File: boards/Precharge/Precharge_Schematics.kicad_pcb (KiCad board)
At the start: 2 copper layers, 67 x 43 mm, 5 parts, among them J1 Ultrafit_2, J2 Ultrafit_2, J3 Ultrafit_2, K1 G2RL-1-E

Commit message: Updated Layout
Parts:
- moved J2 5.53 mm to (178.5, 89.9), turned to 270 degrees
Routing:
- net Low_Side_Drive: track 21.5 -> 7.29 mm
- net Shutdown_in: track 5.04 -> 16.1 mm
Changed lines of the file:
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@@
     (links 5)
     (no_connects 2)
-    (area 123.418599 67.540599 179.359401 114.8118)
+    (area 115.672399 67.247203 182.772401 110.384035)
     (thickness 1.6)
     (drawings 36)
-    (tracks 13)
+    (tracks 14)
     (zones 0)
     (modules 5)
@@
   )
   (setup
-    (last_trace_width 0.254)
+    (last_trace_width 0.762)
     (user_trace_width 0.254)
     (user_trace_width 0.508)
@@
   )
   (module footprints:Ultrafit_2 (layer F.Cu)
-    (at 173.482 87.63 90)
-    (fp_text reference J2 (at 9.0678 0.5917 90) (layer F.SilkS) hide
-      (effects (font (size 1 1) (thickness 0.15)))
-    )
-    (fp_text value Ultrafit_2 (at 4.572 0.508 180) (layer F.Fab) hide
+    (at 178.5366 89.8652 270)
+    (fp_text reference J2 (at 9.0678 0.5917 270) (layer F.SilkS) hide
+      (effects (font (size 1 1) (thickness 0.15)))
+    )
+    (fp_text value Ultrafit_2 (at 4.572 0.508 360) (layer F.Fab) hide
       (effects (font (size 1 1) (thickness 0.15)))
     )
@@
     (fp_line (start -2.54 5.588) (end -5.588 5.588) (layer F.Fab) (width 0.15))
     (fp_line (start -5.588 5.588) (end -5.588 -2.032) (layer F.Fab) (width 0.15))
-    (fp_text user "6.55mm Clearance" (at -4.07 1.75 180) (layer F.Fab) hide
+    (fp_text user "6.55mm Clearance" (at -4.07 1.75 360) (layer F.Fab) hide
       (effects (font (size 0.5 0.5) (thickness 0.08)))
     )
@@
     (fp_line (start -2.42 5.65) (end -2.42 -2.15) (layer F.SilkS) (width 0.15))
     (fp_line (start 3.302 5.65) (end 3.302 -2.15) (layer F.SilkS) (width 0.15))
-    (pad 2 thru_hole circle (at 0 0 90) (size 1.397 1.397) (drill 1.02) (layers *.Cu *.Mask)
+    (pad 2 thru_hole circle (at 0 0 270) (size 1.397 1.397) (drill 1.02) (layers *.Cu *.Mask)
       (net 5 Shutdown_in))
-    (pad 1 thru_hole circle (at 0 3.5 90) (size 1.397 1.397) (drill 1.02) (layers *.Cu *.Mask)
+    (pad 1 thru_hole circle (at 0 3.5 270) (size 1.397 1.397) (drill 1.02) (layers *.Cu *.Mask)
       (net 6 Low_Side_Drive))
-    (pad "" thru_hole circle (at 2.23 1.75 90) (size 1.981 1.981) (drill 1.6) (layers *.Cu *.Mask))
+    (pad "" thru_hole circle (at 2.23 1.75 270) (size 1.981 1.981) (drill 1.6) (layers *.Cu *.Mask))
     (model /home/sherrieshen/Documents/Formula/OEM_Preferred_Parts/3DModels/Ultrafit-2/Ultrafit-2.wrl
       (at (xyz 0 0 0))
@@
     )
   )
-  (gr_text SD_IN (at 173.5709 91.948) (layer F.SilkS)
+  (gr_text SD_IN (at 178.3842 85.9282) (layer F.SilkS)
     (effects (font (size 0.889 0.889) (thickness 0.22225)))
   )
-  (gr_text LSD (at 180.1368 91.8845 90) (layer F.SilkS)
+  (gr_text LSD (at 174.8028 85.7758 90) (layer F.SilkS)
     (effects (font (size 0.889 0.889) (thickness 0.1905)))
   )
@@
   (segment (start 150.346 80.518) (end 150.346 93.323) (width 0.762) (layer F.Cu) (net 3))
   (segment (start 150.346 93.323) (end 153.416 96.393) (width 0.762) (layer F.Cu) (net 3))
-  (segment (start 176.982 100.327) (end 173.416 103.893) (width 0.762) (layer F.Cu) (net 5))
-  (segment (start 173.482 87.63) (end 173.482 96.327) (width 0.762) (layer F.Cu) (net 6))
+  (segment (start 173.416 103.893) (end 178.5366 98.7724) (width 0.762) (layer F.Cu) (net 5))
+  (segment (start 178.5366 98.7724) (end 178.5366 89.8652) (width 0.762) (layer F.Cu) (net 5))
+  (segment (start 175.0366 89.8652) (end 175.0366 94.7724) (width 0.762) (layer F.Cu) (net 6))
+  (segment (start 175.0366 94.7724) (end 173.416 96.393) (width 0.762) (layer F.Cu) (net 6))
   (segment (start 173.482 96.327) (end 173.416 96.393) (width 0.762) (layer F.Cu) (net 6))
-  (segment (start 176.982 87.63) (end 176.982 100.327) (width 0.762) (layer F.Cu) (net 6))
   (segment (start 139.827 99.314) (end 141.058901 98.082099) (width 0.762) (layer F.Cu) (net 8))
   (segment (start 141.058901 98.082099) (end 143.918313 98.082099) (width 0.762) (layer F.Cu) (net 8))

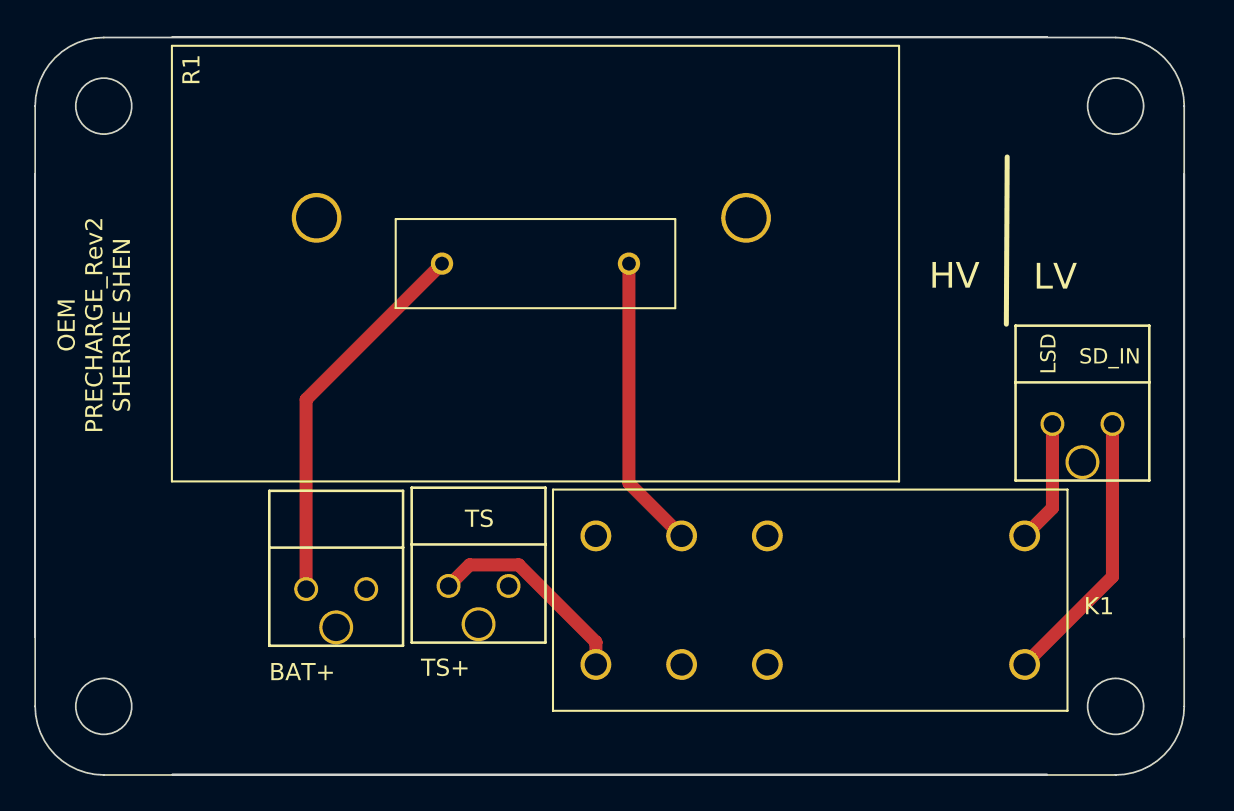
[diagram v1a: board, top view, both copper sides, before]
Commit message: add CAD for precharge
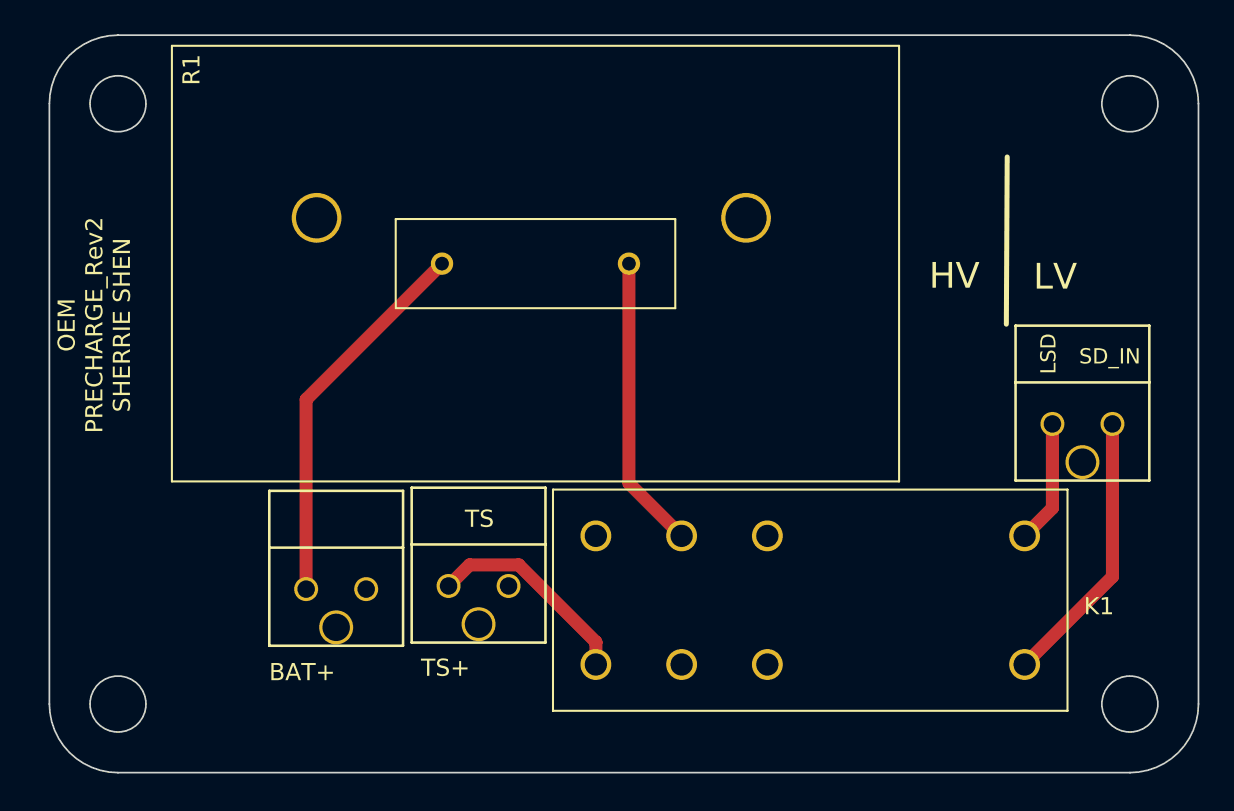
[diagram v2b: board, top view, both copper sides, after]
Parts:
- J1: value Ultrafit_2 -> BAT+
- J2: value Ultrafit_2 -> Shutdown_LSD
- J3: value Ultrafit_2 -> TS+
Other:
- outline, holes or cut-outs redrawn
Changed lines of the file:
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@@
   (general
     (links 5)
-    (no_connects 2)
-    (area 115.672399 67.247203 182.772401 110.384035)
+    (no_connects 0)
+    (area 116.502599 67.147399 183.602601 110.247401)
     (thickness 1.6)
-    (drawings 36)
+    (drawings 32)
     (tracks 14)
     (zones 0)
@@
   )
   (setup
-    (last_trace_width 0.762)
+    (last_trace_width 0.254)
     (user_trace_width 0.254)
     (user_trace_width 0.508)
@@
       (effects (font (size 1 1) (thickness 0.15)))
     )
-    (fp_text value Ultrafit_2 (at 4.572 0.508 360) (layer F.Fab) hide
+    (fp_text value TS+ (at 4.572 0.508 360) (layer F.Fab) hide
       (effects (font (size 1 1) (thickness 0.15)))
     )
@@
       (effects (font (size 1 1) (thickness 0.15)))
     )
-    (fp_text value Ultrafit_2 (at 4.572 0.508 360) (layer F.Fab) hide
+    (fp_text value BAT+ (at 4.572 0.508 360) (layer F.Fab) hide
       (effects (font (size 1 1) (thickness 0.15)))
     )
@@
       (effects (font (size 1 1) (thickness 0.15)))
     )
-    (fp_text value Ultrafit_2 (at 4.572 0.508 360) (layer F.Fab) hide
+    (fp_text value Shutdown_LSD (at 4.572 0.508 360) (layer F.Fab) hide
       (effects (font (size 1 1) (thickness 0.15)))
     )
@@
     )
   )
+  (gr_circle (center 120.5526 71.1974) (end 122.18455 71.1974) (layer Edge.Cuts) (width 0.1))
+  (gr_line (start 183.5526 71.1974) (end 183.5526 106.1974) (layer Edge.Cuts) (width 0.1))
+  (gr_line (start 179.5526 67.1974) (end 120.5526 67.1974) (layer Edge.Cuts) (width 0.1))
+  (gr_circle (center 120.5526 106.1974) (end 122.18455 106.1974) (layer Edge.Cuts) (width 0.1))
+  (gr_arc (start 120.5526 71.1974) (end 120.5526 67.1974) (angle -90) (layer Edge.Cuts) (width 0.1))
+  (gr_arc (start 179.5526 71.1974) (end 183.5526 71.1974) (angle -90) (layer Edge.Cuts) (width 0.1))
+  (gr_circle (center 179.5526 106.1974) (end 181.18455 106.1974) (layer Edge.Cuts) (width 0.1))
+  (gr_arc (start 120.5526 106.1974) (end 116.5526 106.1974) (angle -90) (layer Edge.Cuts) (width 0.1))
+  (gr_line (start 179.5526 110.1974) (end 120.5526 110.1974) (layer Edge.Cuts) (width 0.1))
+  (gr_line (start 116.5526 71.1974) (end 116.5526 106.1974) (layer Edge.Cuts) (width 0.1))
+  (gr_circle (center 179.5526 71.1974) (end 181.18455 71.1974) (layer Edge.Cuts) (width 0.1))
+  (gr_arc (start 179.5526 106.1974) (end 179.5526 110.1974) (angle -90) (layer Edge.Cuts) (width 0.1))
   (gr_text SD_IN (at 178.3842 85.9282) (layer F.SilkS)
     (effects (font (size 0.889 0.889) (thickness 0.22225)))
@@
     (effects (font (size 0.889 0.889) (thickness 0.1905)))
   )
-  (gr_arc (start 178.7224 71.334034) (end 182.7224 71.334034) (angle -90) (layer Edge.Cuts) (width 0.1))
-  (gr_circle (center 178.7224 71.334034) (end 180.35435 71.334034) (layer Edge.Cuts) (width 0.1))
-  (gr_arc (start 178.7224 106.334034) (end 178.7224 110.334034) (angle -90) (layer Edge.Cuts) (width 0.1))
-  (gr_line (start 115.7224 71.334034) (end 115.7224 106.334034) (layer Edge.Cuts) (width 0.1))
-  (gr_line (start 178.7224 67.334034) (end 119.7224 67.334034) (layer Edge.Cuts) (width 0.1))
-  (gr_line (start 182.7224 71.334034) (end 182.7224 106.334034) (layer Edge.Cuts) (width 0.1))
-  (gr_line (start 178.7224 110.334034) (end 119.7224 110.334034) (layer Edge.Cuts) (width 0.1))
-  (gr_circle (center 178.7224 106.334034) (end 180.35435 106.334034) (layer Edge.Cuts) (width 0.1))
-  (gr_arc (start 119.7224 106.334034) (end 115.7224 106.334034) (angle -90) (layer Edge.Cuts) (width 0.1))
-  (gr_circle (center 119.7224 106.334034) (end 121.35435 106.334034) (layer Edge.Cuts) (width 0.1))
-  (gr_arc (start 119.7224 71.334034) (end 119.7224 67.334034) (angle -90) (layer Edge.Cuts) (width 0.1))
-  (gr_circle (center 119.7224 71.334034) (end 121.35435 71.334034) (layer Edge.Cuts) (width 0.1))
-  (gr_line (start 182.7224 75.297204) (end 182.7224 102.297204) (layer Edge.Cuts) (width 0.1))
-  (gr_line (start 174.7224 110.297204) (end 123.7224 110.297204) (layer Edge.Cuts) (width 0.1))
-  (gr_line (start 115.7224 75.297204) (end 115.7224 102.297204) (layer Edge.Cuts) (width 0.1))
-  (gr_line (start 174.7224 67.297204) (end 123.7224 67.297204) (layer Edge.Cuts) (width 0.1))
   (gr_text TS+ (at 139.6492 104.0892) (layer F.SilkS)
     (effects (font (size 1 1) (thickness 0.25)))

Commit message: precharge rev3
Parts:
- moved J1 6.21 mm to (128.8, 99.7)
- moved J3 3.35 mm to (140.0, 99.8)
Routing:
- net TS+: track 12.3 -> 15.2 mm
- net Net-(J1-Pad1): track 22.3 -> 25.0 mm
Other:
- board text added: "OEM PRECHARGE_Rev3 SHERRIE SHEN"
- board text removed: "OEM PRECHARGE_Rev2 SHERRIE SHEN"
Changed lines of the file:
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@@
     (thickness 1.6)
     (drawings 32)
-    (tracks 14)
+    (tracks 13)
     (zones 0)
     (modules 5)
@@
   )
   (setup
-    (last_trace_width 0.254)
+    (last_trace_width 0.762)
     (user_trace_width 0.254)
     (user_trace_width 0.508)
@@
   )
   (module footprints:Ultrafit_2 (layer F.Cu)
-    (at 143.327 99.314 270)
+    (at 140.0149 99.8018 270)
     (fp_text reference J3 (at -13.4672 -0.7646 270) (layer F.SilkS) hide
       (effects (font (size 1 1) (thickness 0.15)))
@@
   )
   (module footprints:Ultrafit_2 (layer F.Cu)
-    (at 135.0238 99.497 270)
+    (at 128.8135 99.6621 270)
     (fp_text reference J1 (at -4.12 -1.044 360) (layer F.SilkS) hide
       (effects (font (size 1 1) (thickness 0.15)))
@@
     (effects (font (size 0.889 0.889) (thickness 0.1905)))
   )
-  (gr_text TS+ (at 139.6492 104.0892) (layer F.SilkS)
+  (gr_text TS+ (at 135.8773 104.7877) (layer F.SilkS)
     (effects (font (size 1 1) (thickness 0.25)))
   )
@@
     (arrow2b (pts (xy 159.390538 107.213431) (xy 160.519351 106.631467)))
   )
-  (gr_text BAT+ (at 131.2926 104.3432) (layer F.SilkS)
+  (gr_text BAT+ (at 125.1966 104.2797) (layer F.SilkS)
     (effects (font (size 1 1) (thickness 0.2)))
   )
-  (gr_text "TS\n" (at 141.6304 95.4024) (layer F.SilkS)
+  (gr_text "TS\n" (at 138.6332 95.7453) (layer F.SilkS)
     (effects (font (size 1 1) (thickness 0.2)))
   )
-  (gr_text "OEM\nPRECHARGE_Rev2\nSHERRIE SHEN" (at 119.1768 84.0994 90) (layer F.SilkS)
+  (gr_text "OEM\nPRECHARGE_Rev3\nSHERRIE SHEN" (at 119.1768 84.0994 90) (layer F.SilkS)
     (effects (font (size 1 1) (thickness 0.2)))
   )
-  (segment (start 131.5238 99.497) (end 131.5238 88.4402) (width 0.762) (layer F.Cu) (net 2))
-  (segment (start 131.5238 88.4402) (end 139.446 80.518) (width 0.762) (layer F.Cu) (net 2))
+  (segment (start 125.3135 99.6621) (end 125.3135 94.6505) (width 0.762) (layer F.Cu) (net 2))
+  (segment (start 125.3135 94.6505) (end 139.446 80.518) (width 0.762) (layer F.Cu) (net 2))
   (segment (start 150.346 80.518) (end 150.346 93.323) (width 0.762) (layer F.Cu) (net 3))
   (segment (start 150.346 93.323) (end 153.416 96.393) (width 0.762) (layer F.Cu) (net 3))
@@
   (segment (start 175.0366 94.7724) (end 173.416 96.393) (width 0.762) (layer F.Cu) (net 6))
   (segment (start 173.482 96.327) (end 173.416 96.393) (width 0.762) (layer F.Cu) (net 6))
-  (segment (start 139.827 99.314) (end 141.058901 98.082099) (width 0.762) (layer F.Cu) (net 8))
-  (segment (start 141.058901 98.082099) (end 143.918313 98.082099) (width 0.762) (layer F.Cu) (net 8))
-  (segment (start 143.918313 98.082099) (end 148.416 102.579786) (width 0.762) (layer F.Cu) (net 8))
-  (segment (start 148.416 102.579786) (end 148.416 102.620208) (width 0.762) (layer F.Cu) (net 8))
-  (segment (start 148.416 102.620208) (end 148.416 103.893) (width 0.762) (layer F.Cu) (net 8))
+  (segment (start 136.5149 99.8018) (end 136.5149 102.537174) (width 0.762) (layer F.Cu) (net 8))
+  (segment (start 136.5149 102.537174) (end 137.870726 103.893) (width 0.762) (layer F.Cu) (net 8))
+  (segment (start 137.870726 103.893) (end 147.143208 103.893) (width 0.762) (layer F.Cu) (net 8))
+  (segment (start 147.143208 103.893) (end 148.416 103.893) (width 0.762) (layer F.Cu) (net 8))
 )

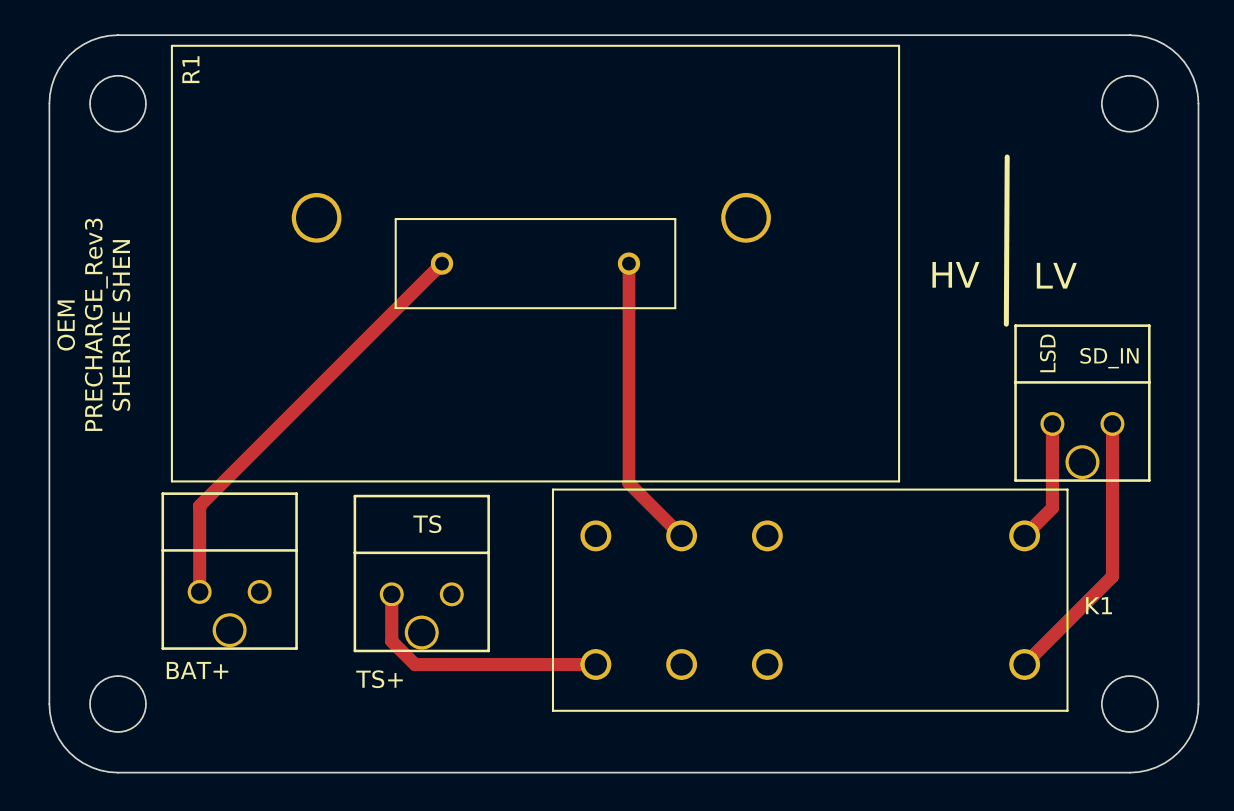
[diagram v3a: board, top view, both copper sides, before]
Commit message: fixed precharge layout
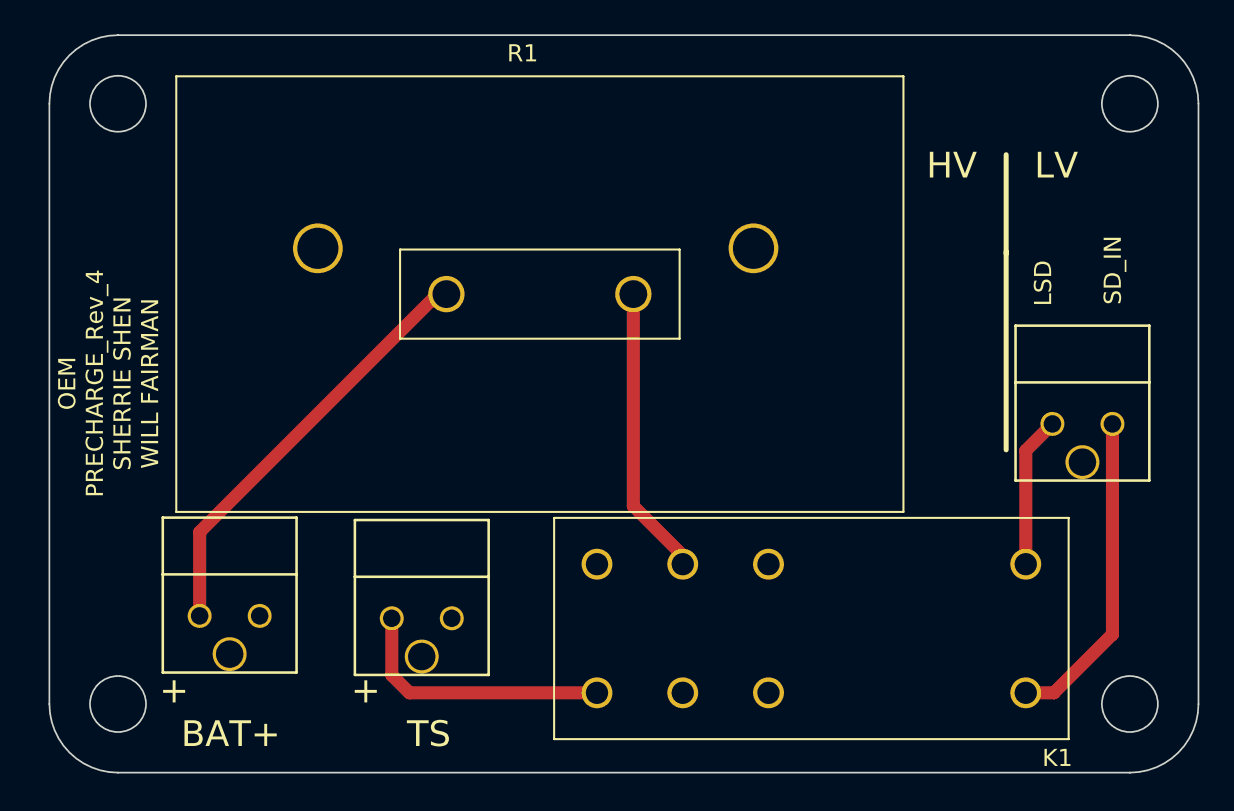
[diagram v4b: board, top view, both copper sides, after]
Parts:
- moved R1 1.80 mm to (139.7, 82.3)
- moved K1 1.65 mm to (173.5, 98.0)
- moved J1 1.40 mm to (128.8, 101.1)
- moved J3 1.40 mm to (140.0, 101.2)
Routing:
- net Shutdown_in: track 16.1 -> 18.7 mm
- net Low_Side_Drive: track 7.29 -> 8.82 mm
- net TS+: track 15.2 -> 15.7 mm
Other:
- board text added: "+"
- board text added: "OEM PRECHARGE_Rev_4 SHERRIE SHEN WILL FAIRMAN"
- board text removed: "0.5060 in"
- board text removed: "OEM PRECHARGE_Rev3 SHERRIE SHEN"
- board text removed: "TS+"
